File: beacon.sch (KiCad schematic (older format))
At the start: 10 parts

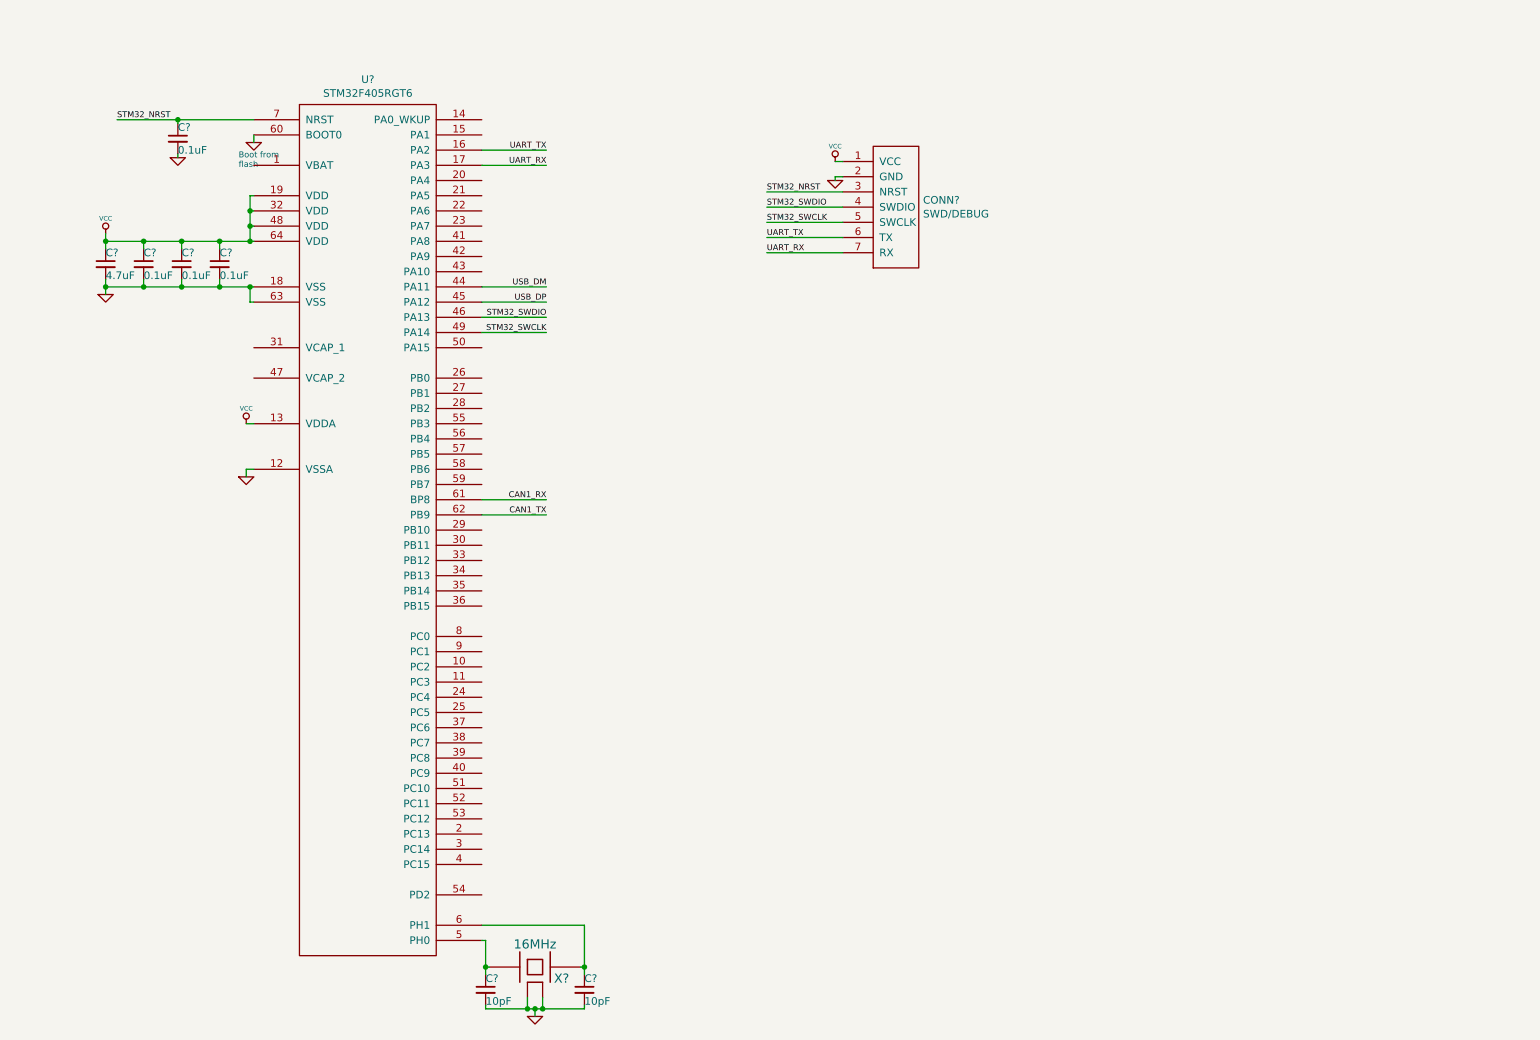
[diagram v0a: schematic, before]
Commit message: Add Decawave 1000 module
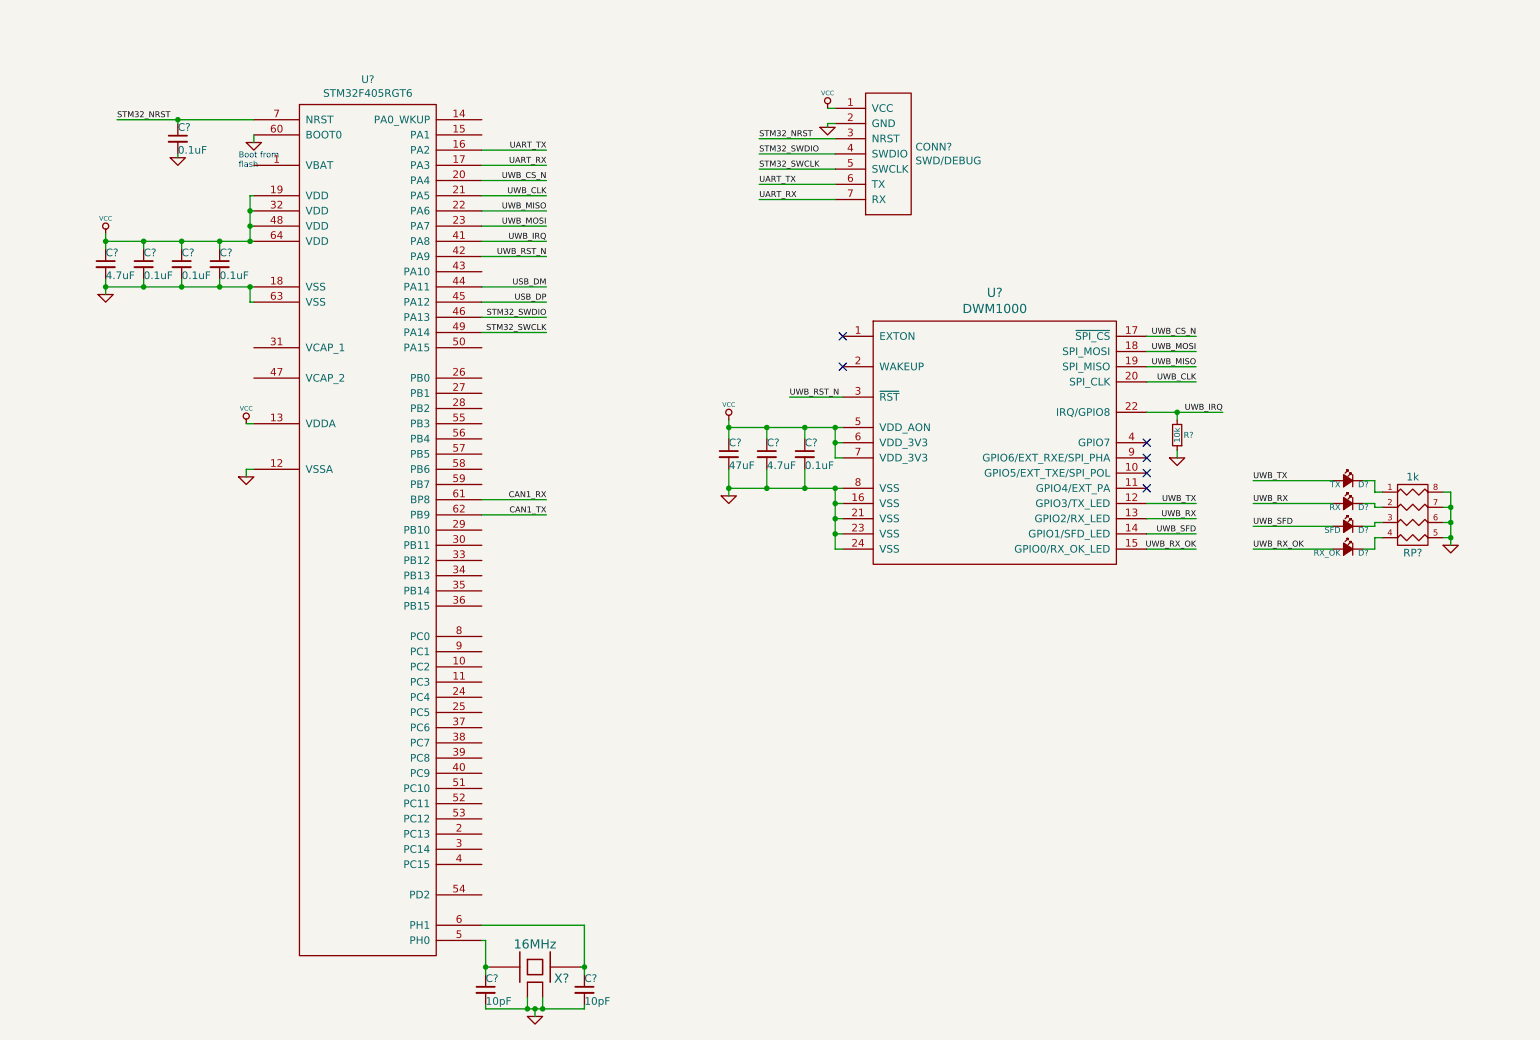
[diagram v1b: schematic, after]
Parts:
- added C?: 0.1uF, symbol C_Small
- added C?: 4.7uF, symbol C_Small
- added C?: 47uF, symbol C_Small
- added D?: TX, symbol Led_Small
- added D?: RX, symbol Led_Small
- added D?: SFD, symbol Led_Small
- added D?: RX_OK, symbol Led_Small
- added R?: 10k, symbol R_Small
- added RP?: 1k, symbol R_PACK4
- added U?: DWM1000, symbol DWM1000
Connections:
- net GND: now also C?.2, C?.2, C?.2, R?.1, RP?.5 (R4), RP?.6 (R3), RP?.7 (R2), RP?.8 (R1), U?.16 (VSS), U?.21 (VSS), U?.23 (VSS), U?.24 (VSS), U?.8 (VSS)
- net VCC: now also C?.1, C?.1, C?.1, U?.5 (VDD_AON), U?.6 (VDD_3V3), U?.7 (VDD_3V3)
- net UWB_CS_N: now reaches U?.20 (PA4)
- net UWB_CS_N: now also U?.17 (~SPI_CS)
- net UWB_CLK: now reaches U?.21 (PA5)
- net UWB_CLK: now also U?.20 (SPI_CLK)
- net UWB_MISO: now reaches U?.22 (PA6)
- net UWB_MISO: now also U?.19 (SPI_MISO)
- net UWB_MOSI: now reaches U?.23 (PA7)
- net UWB_MOSI: now also U?.18 (SPI_MOSI)
- net UWB_IRQ: now reaches U?.41 (PA8)
- net UWB_IRQ: now also R?.2, U?.22 (IRQ/GPIO8)
- net UWB_RST_N: now reaches U?.42 (PA9)
- net UWB_RST_N: now also U?.3 (~RST)
- new net: D?.1 (K), RP?.1 (P1)
- new net: D?.1 (K), RP?.2 (P2)
- new net: D?.1 (K), RP?.3 (P3)
- new net: D?.1 (K), RP?.4 (P4)
- new net UWB_RX: D?.2 (A), U?.13 (GPIO2/RX_LED)
- new net UWB_RX_OK: D?.2 (A), U?.15 (GPIO0/RX_OK_LED)
- new net UWB_SFD: D?.2 (A), U?.14 (GPIO1/SFD_LED)
- new net UWB_TX: D?.2 (A), U?.12 (GPIO3/TX_LED)
- no-connect marks 0 -> 6
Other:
- moved on the sheet: CONN?

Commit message: Add USB
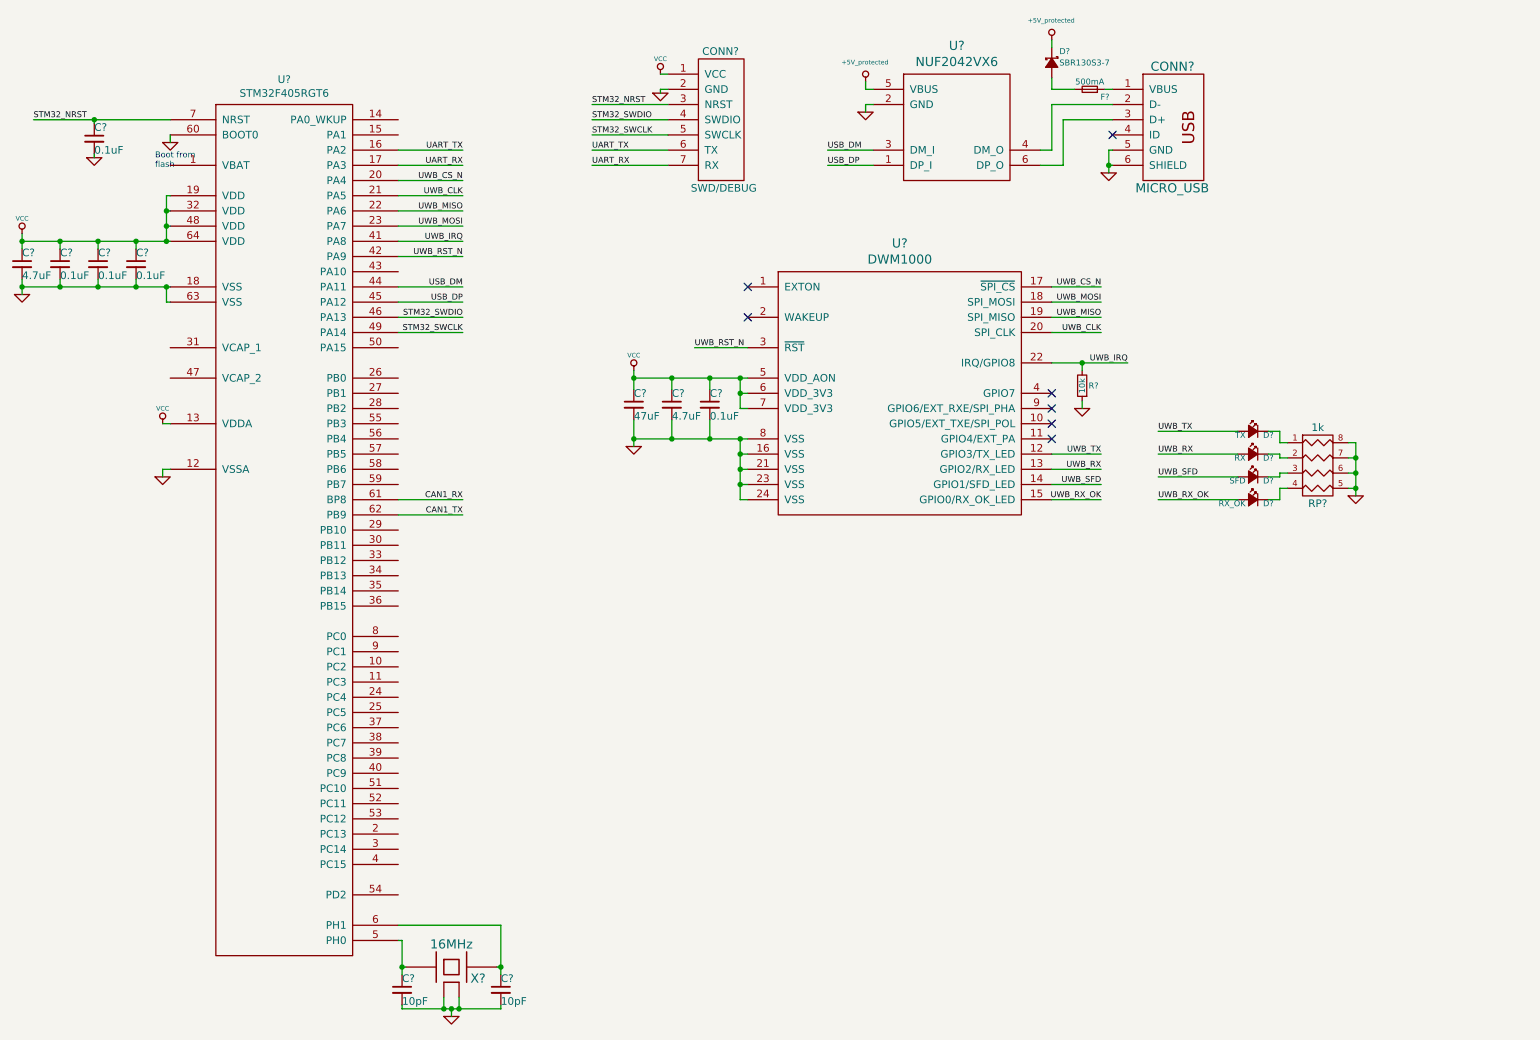
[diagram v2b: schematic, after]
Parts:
- added CONN?: MICRO_USB, symbol MICRO_USB
- added D?: SBR130S3-7, symbol D_Schottky_Small
- added F?: 500mA, symbol F_Small
- added U?: NUF2042VX6, symbol NUF2042VX6
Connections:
- net GND: now also CONN?.5 (GND), CONN?.6 (SHIELD), U?.2 (GND)
- net USB_DM: now also U?.3 (DM_I)
- net USB_DP: now also U?.1 (DP_I)
- new net: CONN?.2 (D-), U?.4 (DM_O)
- new net: CONN?.3 (D+), U?.6 (DP_O)
- new net: CONN?.1 (VBUS), F?.1
- new net: D?.2 (A), F?.2
- new net +5V_protected: D?.1 (K), U?.5 (VBUS)
- no-connect marks 6 -> 7
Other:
- moved on the sheet: C?, CONN?, D?, R?, RP?, U?, X?

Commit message: Add IMU
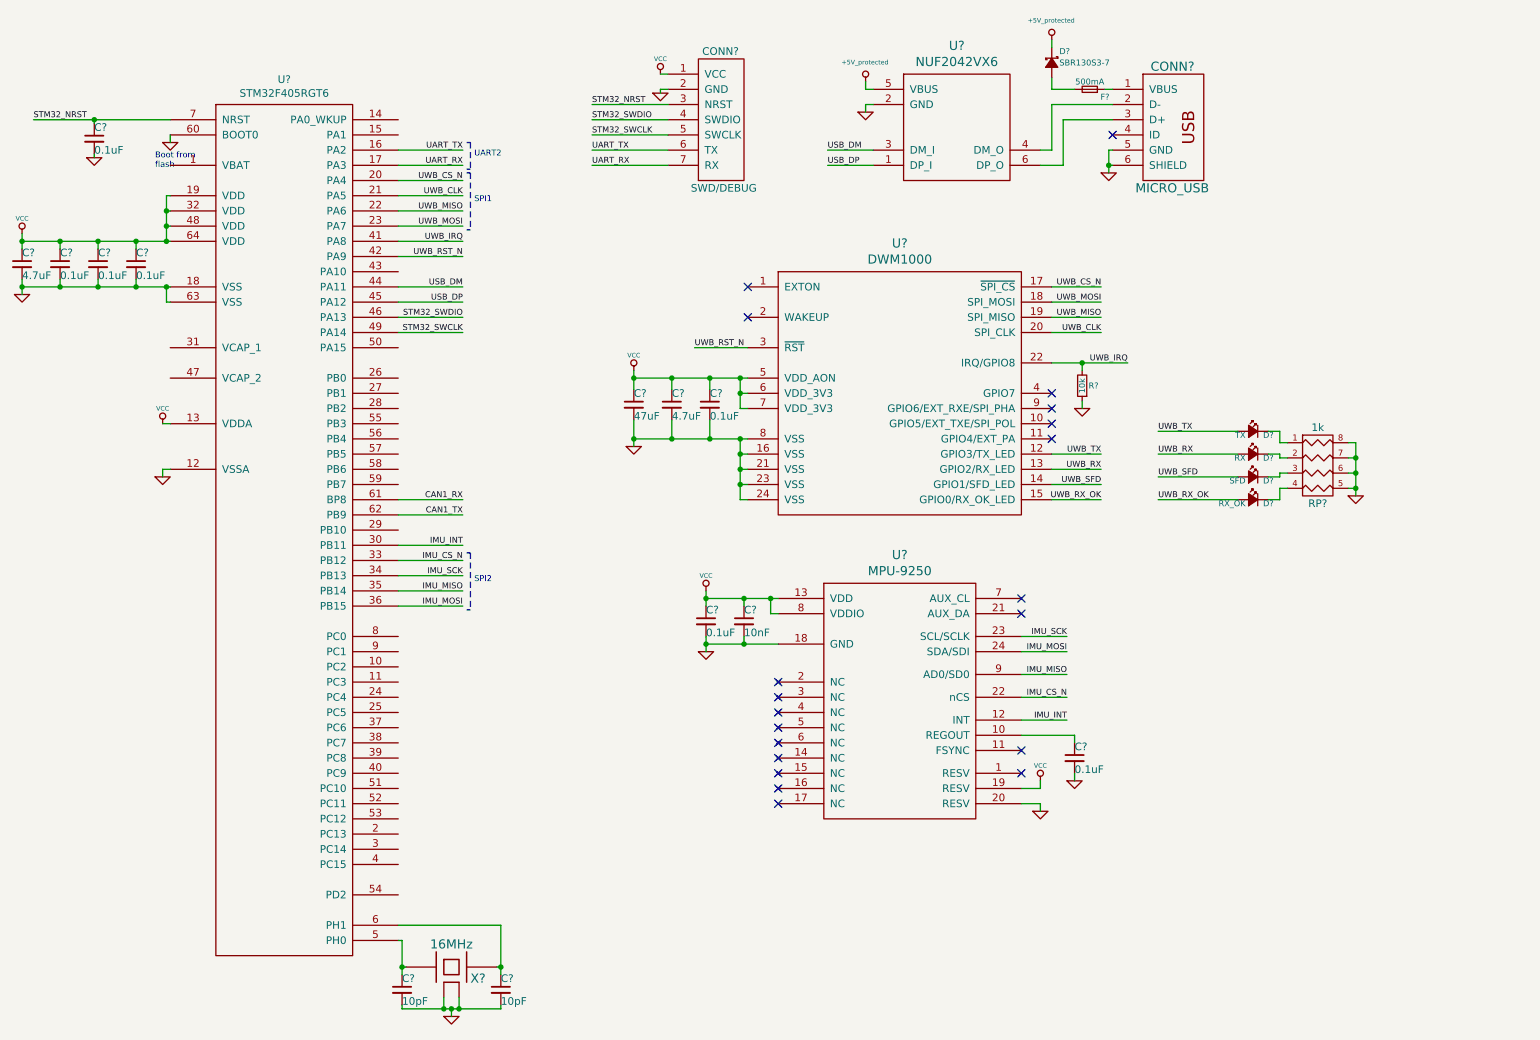
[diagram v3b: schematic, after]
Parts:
- added C?: 10nF, symbol C_Small
- added C? (x2): 0.1uF, symbol C_Small
- added U?: MPU-9250, symbol MPU-9250
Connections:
- net GND: now also C?.2, C?.2, C?.2, U?.18 (GND), U?.20 (RESV)
- net VCC: now also C?.1, C?.1, U?.13 (VDD), U?.19 (RESV), U?.8 (VDDIO)
- net IMU_INT: now reaches U?.30 (PB11)
- net IMU_INT: now also U?.12 (INT)
- net IMU_CS_N: now reaches U?.33 (PB12)
- net IMU_CS_N: now also U?.22 (nCS)
- net IMU_SCK: now reaches U?.34 (PB13)
- net IMU_SCK: now also U?.23 (SCL/SCLK)
- net IMU_MISO: now reaches U?.35 (PB14)
- net IMU_MISO: now also U?.9 (AD0/SD0)
- net IMU_MOSI: now reaches U?.36 (PB15)
- net IMU_MOSI: now also U?.24 (SDA/SDI)
- new net: C?.1, U?.10 (REGOUT)
- no-connect marks 7 -> 20
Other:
- note added: "SPI1"
- note added: "SPI2"
- note added: "UART2"

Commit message: Add CAN interface
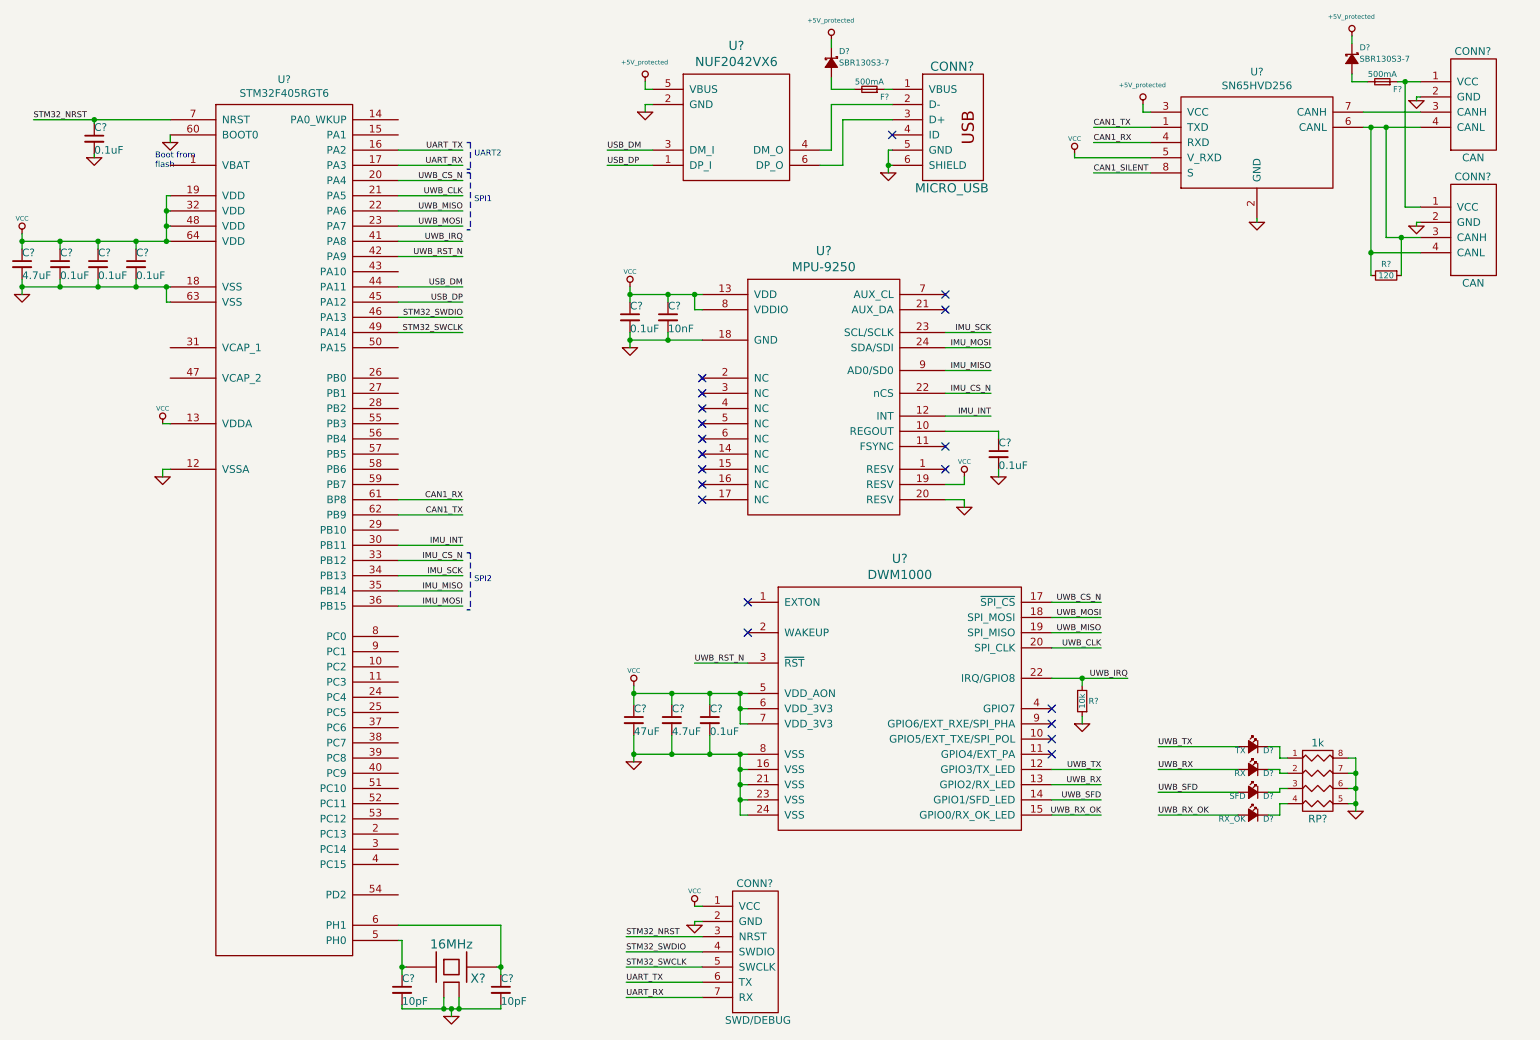
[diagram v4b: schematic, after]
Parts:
- added CONN? (x2): CAN, MODULE, symbol CAN
- added D?: SBR130S3-7, symbol D_Schottky_Small
- added F?: 500mA, symbol F_Small
- added R?: 120, symbol R_Small
- added U?: SN65HVD256, MODULE, symbol SN65HVD256
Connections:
- net +5V_protected: now also D?.1 (K), U?.3 (VCC)
- net CAN1_RX: now also U?.4 (RXD)
- net CAN1_TX: now also U?.1 (TXD)
- net GND: now also CONN?.2 (GND), CONN?.2 (GND), CONN?.MECH (GND), CONN?.MECH (GND), U?.2 (GND)
- net VCC: now also U?.5 (V_RXD)
- new net: CONN?.3 (CANH), CONN?.4 (CANL), CONN?.4 (CANL), R?.1, R?.2, U?.6 (CANL)
- new net: CONN?.3 (CANH), U?.7 (CANH)
- new net: CONN?.1 (VCC), CONN?.1 (VCC), F?.1
- new net: D?.2 (A), F?.2
- new net CAN1_SILENT: U?.8 (S)
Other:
- moved on the sheet: C?, CONN?, D?, F?, R?, RP?, U?
